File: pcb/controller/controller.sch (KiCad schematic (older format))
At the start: 0 parts

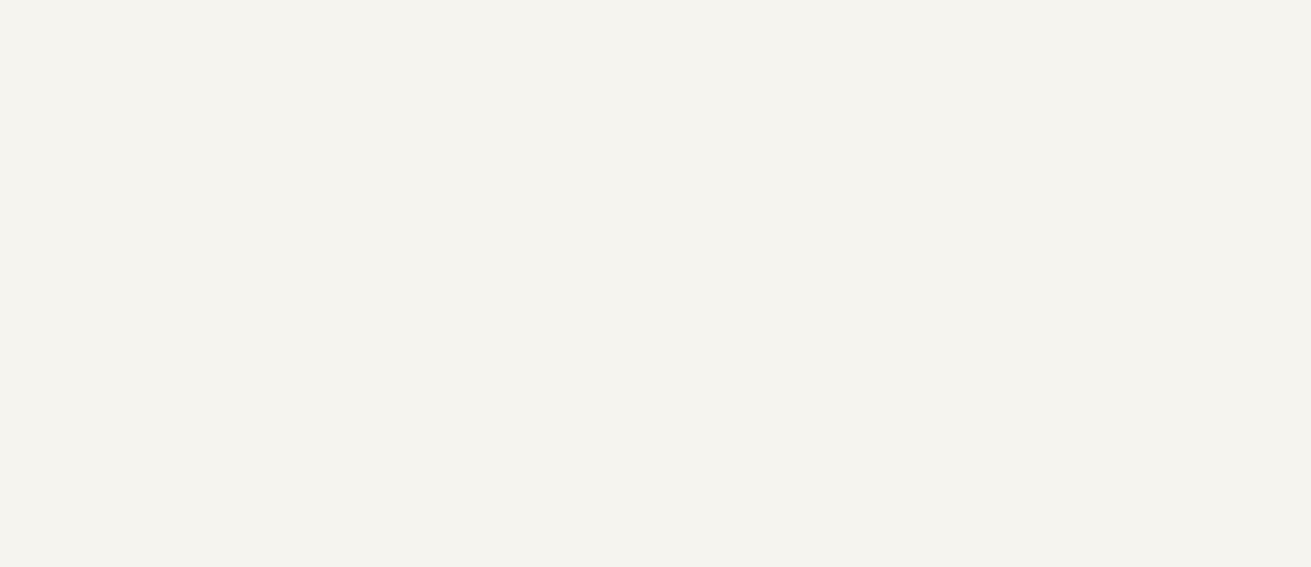
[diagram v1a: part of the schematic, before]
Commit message: pcb component placement almost done
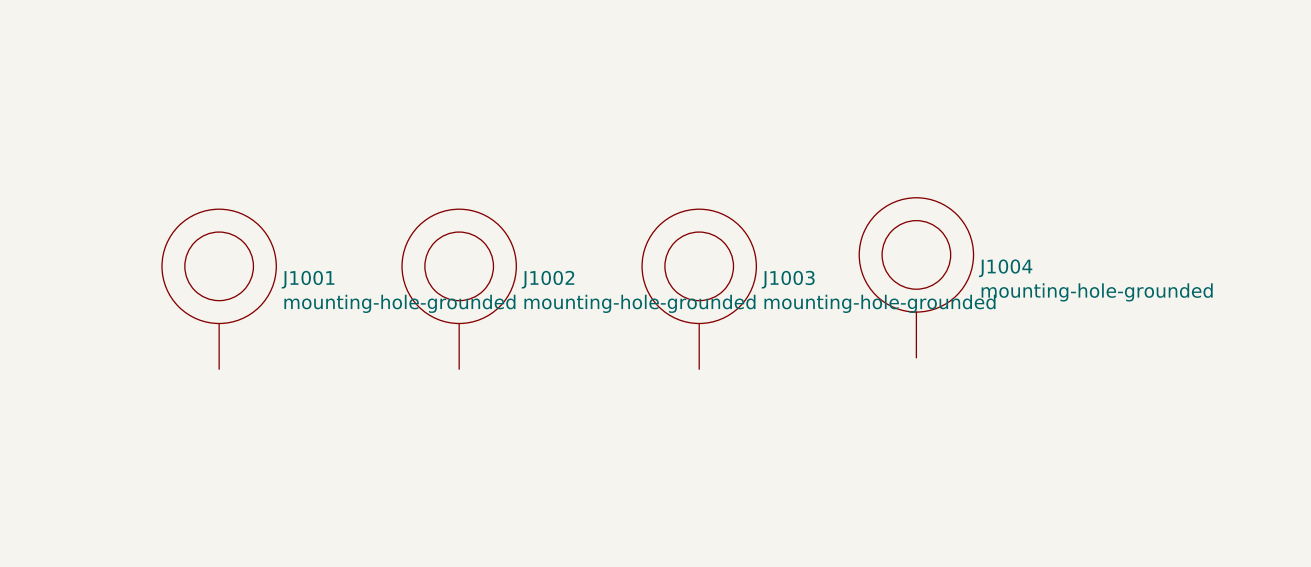
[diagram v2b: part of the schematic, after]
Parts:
- added J1001, J1002, J1003, J1004: mounting-hole-grounded, wbraun_smd:M3-tight-fit-pan-head, symbol wbraun_ic_lib:mounting-hole-grounded
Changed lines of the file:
@@
 F1 "Analog.sch" 50
 $EndSheet
+$Comp
+L wbraun_ic_lib:mounting-hole-grounded J1002
+U 1 1 5C44CD77
+P 6850 4350
+F 0 "J1002" H 7128 4297 60  0000 L CNN
+F 1 "mounting-hole-grounded" H 7128 4191 60  0000 L CNN
+F 2 "wbraun_smd:M3-tight-fit-pan-head" H 6850 4350 60  0001 C CNN
+F 3 "" H 6850 4350 60  0001 C CNN
+	1    6850 4350
+	1    0    0    -1
+$EndComp
+$Comp
+L wbraun_ic_lib:mounting-hole-grounded J1003
+U 1 1 5C44CEBD
+P 7900 4350
+F 0 "J1003" H 8178 4297 60  0000 L CNN
+F 1 "mounting-hole-grounded" H 8178 4191 60  0000 L CNN
+F 2 "wbraun_smd:M3-tight-fit-pan-head" H 7900 4350 60  0001 C CNN
+F 3 "" H 7900 4350 60  0001 C CNN
+	1    7900 4350
+	1    0    0    -1
+$EndComp
+$Comp
+L wbraun_ic_lib:mounting-hole-grounded J1001
+U 1 1 5C44CF0B
+P 5800 4350
+F 0 "J1001" H 6078 4297 60  0000 L CNN
+F 1 "mounting-hole-grounded" H 6078 4191 60  0000 L CNN
+F 2 "wbraun_smd:M3-tight-fit-pan-head" H 5800 4350 60  0001 C CNN
+F 3 "" H 5800 4350 60  0001 C CNN
+	1    5800 4350
+	1    0    0    -1
+$EndComp
+$Comp
+L wbraun_ic_lib:mounting-hole-grounded J1004
+U 1 1 5C44CFC0
+P 8850 4300
+F 0 "J1004" H 9128 4247 60  0000 L CNN
+F 1 "mounting-hole-grounded" H 9128 4141 60  0000 L CNN
+F 2 "wbraun_smd:M3-tight-fit-pan-head" H 8850 4300 60  0001 C CNN
+F 3 "" H 8850 4300 60  0001 C CNN
+	1    8850 4300
+	1    0    0    -1
+$EndComp
 $EndSCHEMATC

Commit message: controller layout done and schematic reviewed
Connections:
- net GND: now reaches J1002.1
- net GND: now also J1001.1, J1003.1, J1004.1
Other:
- moved on the sheet: J1004
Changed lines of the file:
@@
 L wbraun_ic_lib:mounting-hole-grounded J1004
 U 1 1 5C44CFC0
-P 8850 4300
-F 0 "J1004" H 9128 4247 60  0000 L CNN
-F 1 "mounting-hole-grounded" H 9128 4141 60  0000 L CNN
-F 2 "wbraun_smd:M3-tight-fit-pan-head" H 8850 4300 60  0001 C CNN
-F 3 "" H 8850 4300 60  0001 C CNN
-	1    8850 4300
+P 8850 4350
+F 0 "J1004" H 9128 4297 60  0000 L CNN
+F 1 "mounting-hole-grounded" H 9128 4191 60  0000 L CNN
+F 2 "wbraun_smd:M3-tight-fit-pan-head" H 8850 4350 60  0001 C CNN
+F 3 "" H 8850 4350 60  0001 C CNN
+	1    8850 4350
 	1    0    0    -1
 $EndComp
+$Comp
+L power:GND #PWR0203
+U 1 1 5C4A8EAE
+P 5800 4950
+F 0 "#PWR0203" H 5800 4700 50  0001 C CNN
+F 1 "GND" H 5805 4777 50  0000 C CNN
+F 2 "" H 5800 4950 50  0001 C CNN
+F 3 "" H 5800 4950 50  0001 C CNN
+	1    5800 4950
+	1    0    0    -1
+$EndComp
+$Comp
+L power:GND #PWR0204
+U 1 1 5C4A8ED0
+P 6850 4950
+F 0 "#PWR0204" H 6850 4700 50  0001 C CNN
+F 1 "GND" H 6855 4777 50  0000 C CNN
+F 2 "" H 6850 4950 50  0001 C CNN
+F 3 "" H 6850 4950 50  0001 C CNN
+	1    6850 4950
+	1    0    0    -1
+$EndComp
+$Comp
+L power:GND #PWR0216
+U 1 1 5C4A8EE3
+P 7900 4950
+F 0 "#PWR0216" H 7900 4700 50  0001 C CNN
+F 1 "GND" H 7905 4777 50  0000 C CNN
+F 2 "" H 7900 4950 50  0001 C CNN
+F 3 "" H 7900 4950 50  0001 C CNN
+	1    7900 4950
+	1    0    0    -1
+$EndComp
+$Comp
+L power:GND #PWR0217
+U 1 1 5C4A8EF6
+P 8850 4950
+F 0 "#PWR0217" H 8850 4700 50  0001 C CNN
+F 1 "GND" H 8855 4777 50  0000 C CNN
+F 2 "" H 8850 4950 50  0001 C CNN
+F 3 "" H 8850 4950 50  0001 C CNN
+	1    8850 4950
+	1    0    0    -1
+$EndComp
+Wire Wire Line
+	5800 4800 5800 4950
+Wire Wire Line
+	6850 4800 6850 4950
+Wire Wire Line
+	7900 4800 7900 4950
+Wire Wire Line
+	8850 4800 8850 4950
 $EndSCHEMATC
